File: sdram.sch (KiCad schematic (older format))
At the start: 2 parts, among them U1 LFE5U-12F-8BG256C, U17 IS42S16400J-xT

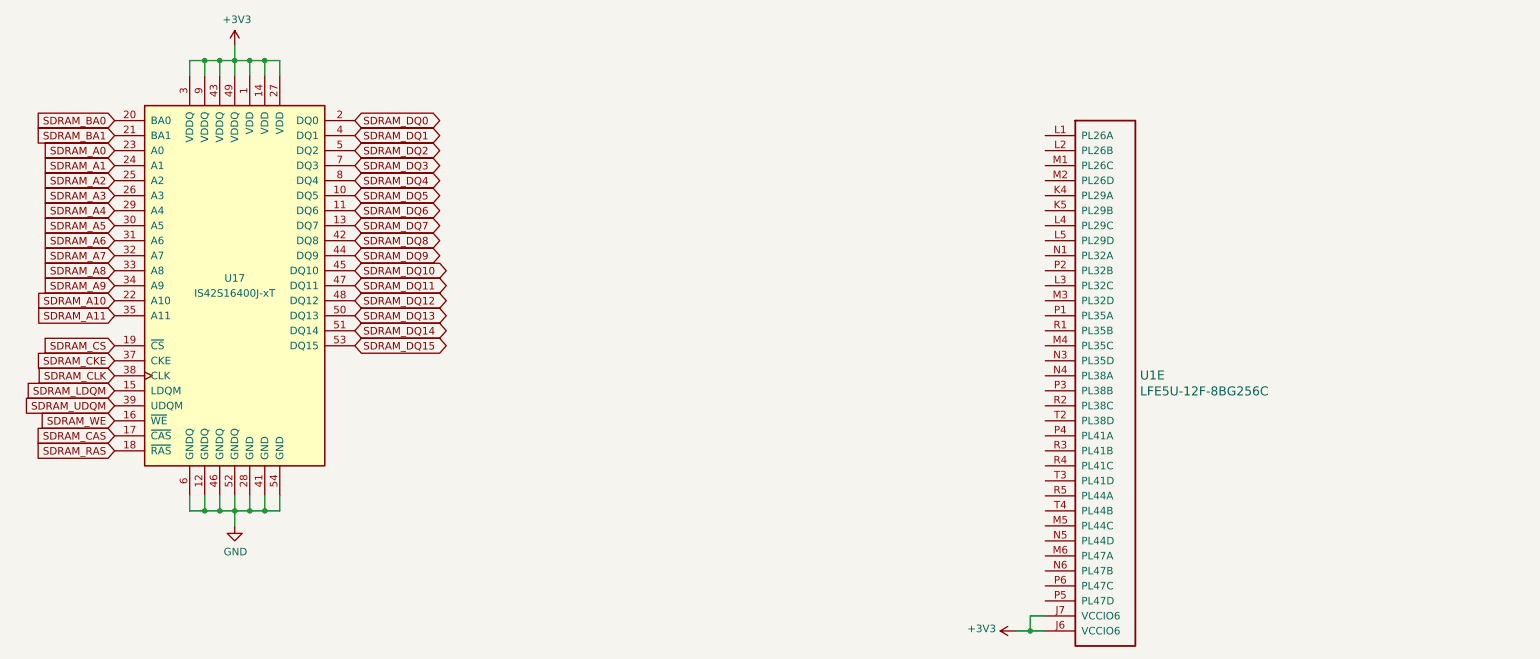
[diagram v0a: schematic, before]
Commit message: add sdram connections
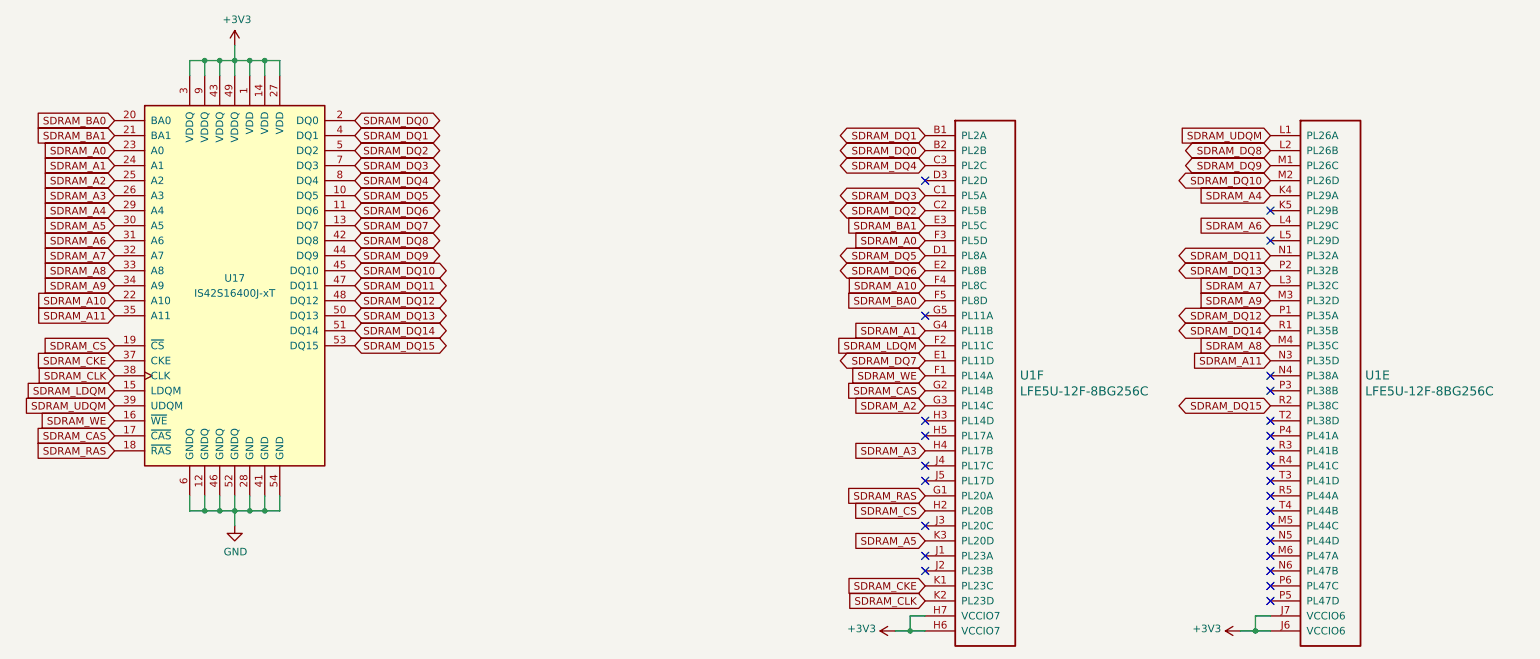
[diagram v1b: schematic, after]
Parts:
- added unit 6 of U1
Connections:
- net +3V3: now also U1.H6 (VCCIO7), U1.H7 (VCCIO7)
- net SDRAM_A0: now also U1.F3 (PL5D)
- net SDRAM_A1: now also U1.G4 (PL11B)
- net SDRAM_A10: now also U1.F4 (PL8C)
- net SDRAM_A11: now also U1.N3 (PL35D)
- net SDRAM_A2: now also U1.G3 (PL14C)
- net SDRAM_A3: now also U1.H4 (PL17B)
- net SDRAM_A4: now also U1.K4 (PL29A)
- net SDRAM_A5: now also U1.K3 (PL20D)
- net SDRAM_A6: now also U1.L4 (PL29C)
- net SDRAM_A7: now also U1.L3 (PL32C)
- net SDRAM_A8: now also U1.M4 (PL35C)
- net SDRAM_A9: now also U1.M3 (PL32D)
- net SDRAM_BA0: now also U1.F5 (PL8D)
- net SDRAM_BA1: now also U1.E3 (PL5C)
- net SDRAM_CAS: now also U1.G2 (PL14B)
- net SDRAM_CKE: now also U1.K1 (PL23C)
- net SDRAM_CLK: now also U1.K2 (PL23D)
- net SDRAM_CS: now also U1.H2 (PL20B)
- net SDRAM_DQ0: now also U1.B2 (PL2B)
- net SDRAM_DQ1: now also U1.B1 (PL2A)
- net SDRAM_DQ10: now also U1.M2 (PL26D)
- net SDRAM_DQ11: now also U1.N1 (PL32A)
- net SDRAM_DQ12: now also U1.P1 (PL35A)
- net SDRAM_DQ13: now also U1.P2 (PL32B)
- net SDRAM_DQ14: now also U1.R1 (PL35B)
- net SDRAM_DQ15: now also U1.R2 (PL38C)
- net SDRAM_DQ2: now also U1.C2 (PL5B)
- net SDRAM_DQ3: now also U1.C1 (PL5A)
- net SDRAM_DQ4: now also U1.C3 (PL2C)
- net SDRAM_DQ5: now also U1.D1 (PL8A)
- net SDRAM_DQ6: now also U1.E2 (PL8B)
- net SDRAM_DQ7: now also U1.E1 (PL11D)
- net SDRAM_DQ8: now also U1.L2 (PL26B)
- net SDRAM_DQ9: now also U1.M1 (PL26C)
- net SDRAM_LDQM: now also U1.F2 (PL11C)
- net SDRAM_RAS: now also U1.G1 (PL20A)
- net SDRAM_UDQM: now also U1.L1 (PL26A)
- net SDRAM_WE: now also U1.F1 (PL14A)
- no-connect marks 0 -> 26
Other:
- moved on the sheet: U1E
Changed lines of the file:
@@
 	2400 1300 2500 1300
 Wire Wire Line
-	8000 5000 7900 5000
+	9500 5000 9400 5000
 Wire Wire Line
-	7900 5000 7900 5100
+	9400 5000 9400 5100
 Wire Wire Line
-	8000 5100 7900 5100
+	9500 5100 9400 5100
 $Comp
 L ecp5:LFE5U-12F-8BG256C U?
 U 5 1 5C30D379
-P 8000 1800
+P 9500 1800
 AR Path="/5C254FCC/5C30D379" Ref="U?"  Part="5"
 AR Path="/5C35F270/5C30D379" Ref="U?"  Part="5"
 AR Path="/5C30D379" Ref="U?"  Part="5"
 AR Path="/5C2FB052/5C30D379" Ref="U1"  Part="5"
-F 0 "U1" H 8631 203 60  0000 L CNN
-F 1 "LFE5U-12F-8BG256C" H 8631 97  60  0000 L CNN
-F 2 "Package_BGA:BGA-256_14.0x14.0mm_Layout16x16_P0.8mm_Ball0.45mm_Pad0.32mm_NSMD" H 8200 1850 60  0001 L CNN
-F 3 "" H 8000 1800 50  0001 C CNN
-	5    8000 1800
+F 0 "U1" H 10131 203 60  0000 L CNN
+F 1 "LFE5U-12F-8BG256C" H 10131 97  60  0000 L CNN
+F 2 "Package_BGA:BGA-256_14.0x14.0mm_Layout16x16_P0.8mm_Ball0.45mm_Pad0.32mm_NSMD" H 9700 1850 60  0001 L CNN
+F 3 "" H 9500 1800 50  0001 C CNN
+	5    9500 1800
 	1    0    0    -1
 $EndComp
 Wire Wire Line
-	7800 5100 7900 5100
-Connection ~ 7900 5100
+	9300 5100 9400 5100
+Connection ~ 9400 5100
 $Comp
 L power:+3V3 #PWR?
 U 1 1 5C30D38B
-P 7800 5100
+P 9300 5100
 AR Path="/5C35F270/5C30D38B" Ref="#PWR?"  Part="1"
 AR Path="/5C30D38B" Ref="#PWR?"  Part="1"
 AR Path="/5C2FB052/5C30D38B" Ref="#PWR0165"  Part="1"
-F 0 "#PWR0165" H 7800 4950 50  0001 C CNN
-F 1 "+3V3" V 7815 5228 50  0000 L CNN
-F 2 "" H 7800 5100 50  0001 C CNN
-F 3 "" H 7800 5100 50  0001 C CNN
-	1    7800 5100
+F 0 "#PWR0165" H 9300 4950 50  0001 C CNN
+F 1 "+3V3" V 9315 5228 50  0000 L CNN
+F 2 "" H 9300 5100 50  0001 C CNN
+F 3 "" H 9300 5100 50  0001 C CNN
+	1    9300 5100
 	0    -1   -1   0
 $EndComp
 Wire Wire Line
 	2300 1400 2300 1300
+Wire Wire Line
+	7200 5000 7100 5000
+Wire Wire Line
+	7100 5000 7100 5100
+Wire Wire Line
+	7200 5100 7100 5100
+$Comp
+L ecp5:LFE5U-12F-8BG256C U?
+U 6 1 5C362696
+P 7200 1800
+AR Path="/5C254FCC/5C362696" Ref="U?"  Part="6"
+AR Path="/5C35F270/5C362696" Ref="U?"  Part="6"
+AR Path="/5C362696" Ref="U?"  Part="6"
+AR Path="/5C2FB052/5C362696" Ref="U1"  Part="6"
+AR Path="/5C254FC9/5C362696" Ref="U?"  Part="6"
+F 0 "U1" H 7831 203 60  0000 L CNN
+F 1 "LFE5U-12F-8BG256C" H 7831 97  60  0000 L CNN
+F 2 "Package_BGA:BGA-256_14.0x14.0mm_Layout16x16_P0.8mm_Ball0.45mm_Pad0.32mm_NSMD" H 7400 1850 60  0001 L CNN
+F 3 "" H 7200 1800 50  0001 C CNN
+	6    7200 1800
+	1    0    0    -1
+$EndComp
+Wire Wire Line
+	7000 5100 7100 5100
+Connection ~ 7100 5100
+$Comp
+L power:+3V3 #PWR?
+U 1 1 5C36269F
+P 7000 5100
+AR Path="/5C35F270/5C36269F" Ref="#PWR?"  Part="1"
+AR Path="/5C36269F" Ref="#PWR?"  Part="1"
+AR Path="/5C2FB052/5C36269F" Ref="#PWR0166"  Part="1"
+AR Path="/5C254FC9/5C36269F" Ref="#PWR?"  Part="1"
+F 0 "#PWR0166" H 7000 4950 50  0001 C CNN
+F 1 "+3V3" V 7015 5228 50  0000 L CNN
+F 2 "" H 7000 5100 50  0001 C CNN
+F 3 "" H 7000 5100 50  0001 C CNN
+	1    7000 5100
+	0    -1   -1   0
+$EndComp
+Text GLabel 7200 1900 0    50   BiDi ~ 0
+SDRAM_DQ0
+Text GLabel 7200 1800 0    50   BiDi ~ 0
+SDRAM_DQ1
+Text GLabel 7200 2300 0    50   BiDi ~ 0
+SDRAM_DQ2
+Text GLabel 7200 2200 0    50   BiDi ~ 0
+SDRAM_DQ3
+Text GLabel 7200 2000 0    50   BiDi ~ 0
+SDRAM_DQ4
+Text GLabel 7200 2600 0    50   BiDi ~ 0
+SDRAM_DQ5
+Text GLabel 7200 2700 0    50   BiDi ~ 0
+SDRAM_DQ6
+Text GLabel 7200 3300 0    50   BiDi ~ 0
+SDRAM_DQ7
+Text GLabel 9500 1900 0    50   BiDi ~ 0
+SDRAM_DQ8
+Text GLabel 9500 2000 0    50   BiDi ~ 0
+SDRAM_DQ9
+Text GLabel 9500 2100 0    50   BiDi ~ 0
+SDRAM_DQ10
+Text GLabel 9500 2600 0    50   BiDi ~ 0
+SDRAM_DQ11
+Text GLabel 9500 3000 0    50   BiDi ~ 0
+SDRAM_DQ12
+Text GLabel 9500 2700 0    50   BiDi ~ 0
+SDRAM_DQ13
+Text GLabel 9500 3100 0    50   BiDi ~ 0
+SDRAM_DQ14
+Text GLabel 9500 3600 0    50   BiDi ~ 0
+SDRAM_DQ15
+Text GLabel 7200 2500 0    50   Input ~ 0
+SDRAM_A0
+Text GLabel 7200 3100 0    50   Input ~ 0
+SDRAM_A1
+Text GLabel 7200 3600 0    50   Input ~ 0
+SDRAM_A2
+Text GLabel 7200 3900 0    50   Input ~ 0
+SDRAM_A3
+Text GLabel 9500 2200 0    50   Input ~ 0
+SDRAM_A4
+Text GLabel 7200 4500 0    50   Input ~ 0
+SDRAM_A5
+Text GLabel 9500 2400 0    50   Input ~ 0
+SDRAM_A6
+Text GLabel 9500 2800 0    50   Input ~ 0
+SDRAM_A7
+Text GLabel 9500 3200 0    50   Input ~ 0
+SDRAM_A8
+Text GLabel 9500 2900 0    50   Input ~ 0
+SDRAM_A9
+Text GLabel 7200 2800 0    50   Input ~ 0
+SDRAM_A10
+Text GLabel 9500 3300 0    50   Input ~ 0
+SDRAM_A11
+Text GLabel 7200 2900 0    50   Input ~ 0
+SDRAM_BA0
+Text GLabel 7200 2400 0    50   Input ~ 0
+SDRAM_BA1
+Text GLabel 7200 4300 0    50   Input ~ 0
+SDRAM_CS
+Text GLabel 7200 4800 0    50   Input ~ 0
+SDRAM_CKE
+Text GLabel 7200 4900 0    50   Input ~ 0
+SDRAM_CLK
+Text GLabel 7200 3200 0    50   Input ~ 0
+SDRAM_LDQM
+Text GLabel 9500 1800 0    50   Input ~ 0
+SDRAM_UDQM
+Text GLabel 7200 3400 0    50   Input ~ 0
+SDRAM_WE
+Text GLabel 7200 3500 0    50   Input ~ 0
+SDRAM_CAS
+Text GLabel 7200 4200 0    50   Input ~ 0
+SDRAM_RAS
+NoConn ~ 7200 3000
+NoConn ~ 7200 3700
+NoConn ~ 7200 3800
+NoConn ~ 7200 4000
+NoConn ~ 7200 4100
+NoConn ~ 7200 4400
+NoConn ~ 7200 4600
+NoConn ~ 7200 4700
+NoConn ~ 9500 3400
+NoConn ~ 9500 3500
+NoConn ~ 9500 3700
+NoConn ~ 9500 3800
+NoConn ~ 9500 3900
+NoConn ~ 9500 4000
+NoConn ~ 9500 4100
+NoConn ~ 9500 4200
+NoConn ~ 9500 4300
+NoConn ~ 9500 4400
+NoConn ~ 9500 4500
+NoConn ~ 9500 4600
+NoConn ~ 9500 4700
+NoConn ~ 9500 4800
+NoConn ~ 9500 4900
+NoConn ~ 9500 2300
+NoConn ~ 9500 2500
+NoConn ~ 7200 2100
 $EndSCHEMATC

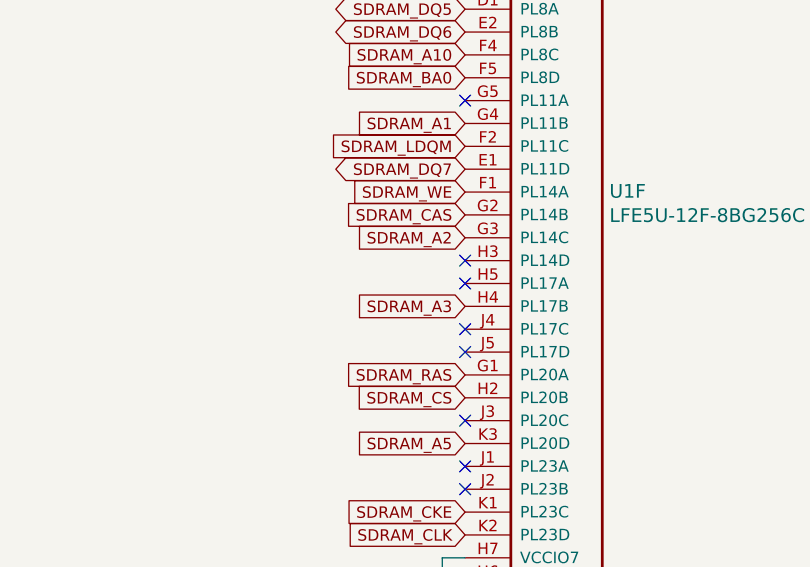
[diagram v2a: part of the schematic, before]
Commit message: small pin change in sdram
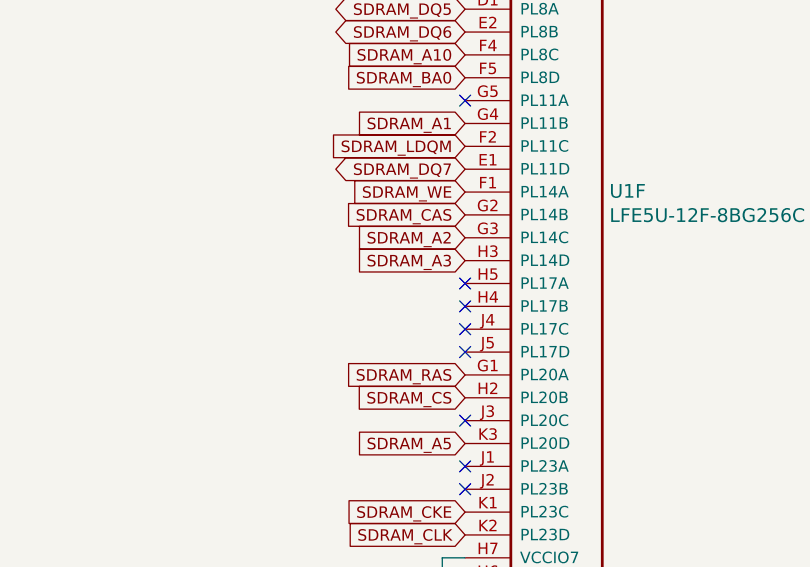
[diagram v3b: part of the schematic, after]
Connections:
- net SDRAM_A3: now also U1.H3 (PL14D); no longer U1.H4 (PL17B)
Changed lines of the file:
@@
 Text GLabel 7200 3600 0    50   Input ~ 0
 SDRAM_A2
-Text GLabel 7200 3900 0    50   Input ~ 0
+Text GLabel 7200 3700 0    50   Input ~ 0
 SDRAM_A3
 Text GLabel 9500 2200 0    50   Input ~ 0
@@
 SDRAM_RAS
 NoConn ~ 7200 3000
-NoConn ~ 7200 3700
 NoConn ~ 7200 3800
 NoConn ~ 7200 4000
@@
 NoConn ~ 9500 2500
 NoConn ~ 7200 2100
+NoConn ~ 7200 3900
 $EndSCHEMATC
